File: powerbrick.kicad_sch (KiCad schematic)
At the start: 10 parts, among them J13 Conn_01x02_Socket, U4 LM2596S-3.3, U7 AMS1117-3.3

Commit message: .
.
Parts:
- added C18, C19, C20, C22, C23: 220nF/6,3V, Capacitor_SMD:C_0603_1608Metric, symbol Device:C
- added J17: Conn_01x02_Socket, Connector_JST:JST_XH_B2B-XH-A_1x02_P2.50mm_Vertical, symbol Connector:Conn_01x02_Socket
- added R13, R24, R25, R27: 10k, Resistor_SMD:R_0603_1608Metric, symbol Device:R
- added R26: 20k, Resistor_SMD:R_0603_1608Metric, symbol Device:R
- added TH1: Thermistor_NTC, Resistor_THT:R_Axial_DIN0204_L3.6mm_D1.6mm_P2.54mm_Vertical, symbol Device:Thermistor_NTC
- added U11, U13: AMS1117-3.3, Package_TO_SOT_SMD:SOT-223-3_TabPin2, symbol Regulator_Linear:AMS1117-3.3
- added U12: TP4056-42-ESOP8, Package_SO:SOIC-8-1EP_3.9x4.9mm_P1.27mm_EP2.41x3.3mm_ThermalVias, symbol Battery_Management:TP4056-42-ESOP8
- J13: footprint (none) -> Connector_Phoenix_MC:PhoenixContact_MC_1,5_2-GF-3.5_1x02_P3.50mm_Horizontal_ThreadedFlange_MountHole
- L1: value L -> 33uH; footprint (none) -> Inductor_SMD:L_7.3x7.3_H4.5
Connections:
- net +3.3V: now also C19.1, C23.1, U11.2 (VO), U13.2 (VO)
- net +5V: now also R24.1, R27.1, U12.4 (V_{CC}), U12.8 (CE)
- net GND: now also C18.2, C19.2, C20.2, C22.2, C23.2, J17.2 (Pin_2), R13.2, R25.2, R26.2, TH1.2, U11.1 (GND), U12.3 (GND), U12.9 (EPAD), U13.1 (GND)
- new net: R24.2, R25.1, TH1.1, U12.1 (TEMP)
- new net: R13.1, U12.2 (PROG)
- new net +BATT: C18.1, C20.1, C22.1, J17.1 (Pin_1), U11.3 (VI), U12.5 (BAT), U13.3 (VI)
- new net Vbat: R26.1, R27.2

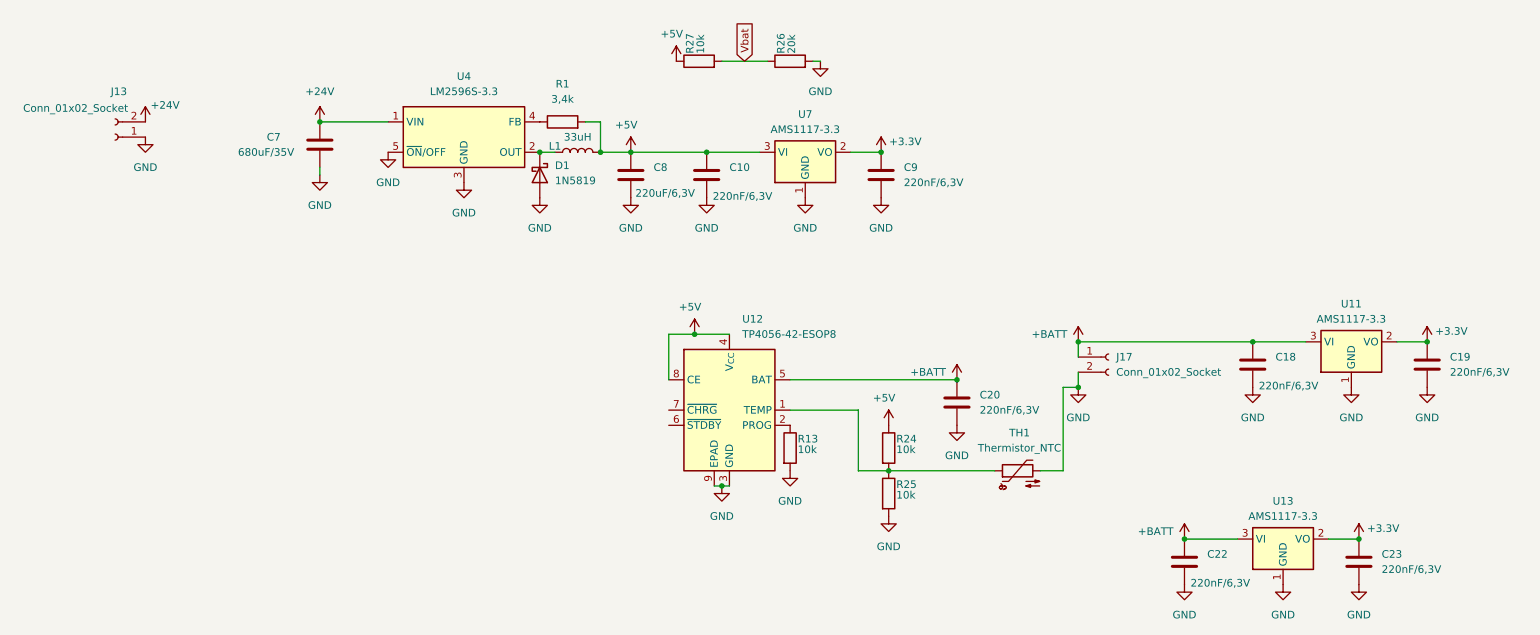
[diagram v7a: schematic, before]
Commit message: RIP
reason of death
too much of board for too little time...
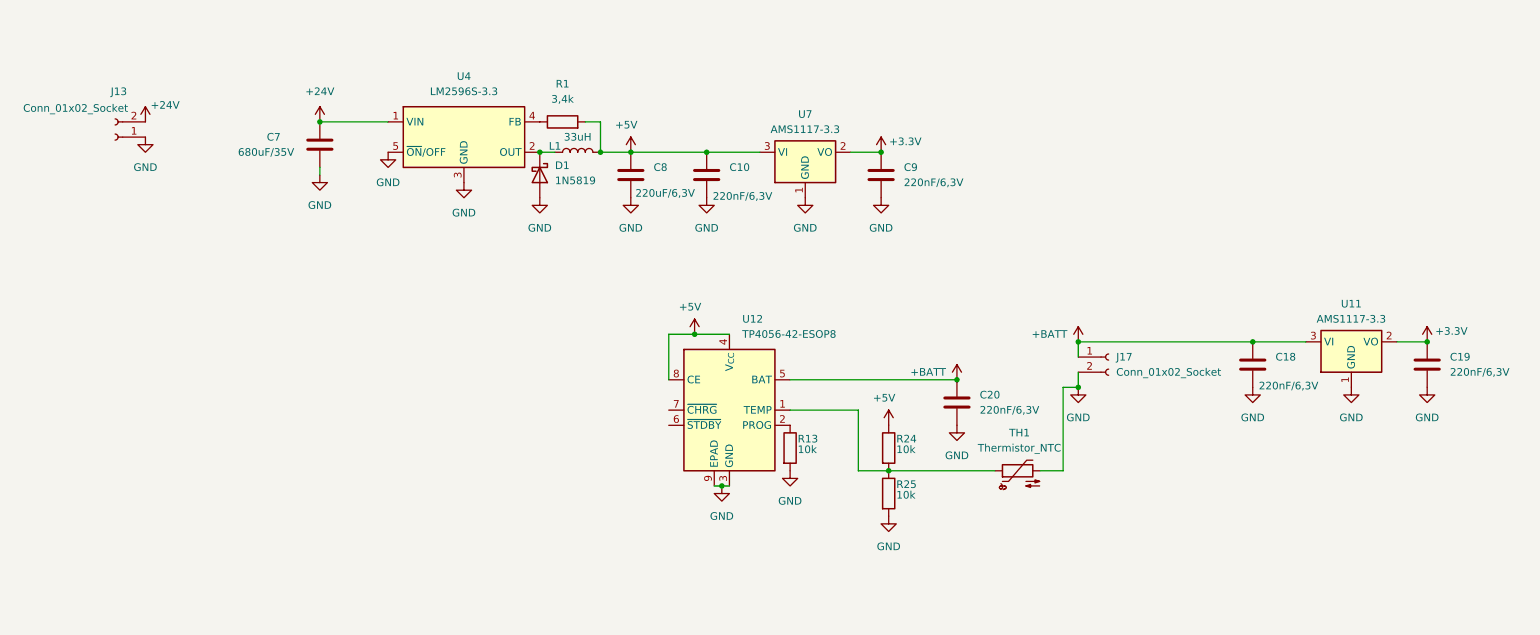
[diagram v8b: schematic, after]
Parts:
- removed C22, C23: 220nF/6,3V, Capacitor_SMD:C_0603_1608Metric, symbol Device:C
- removed R26: 20k, Resistor_SMD:R_0603_1608Metric, symbol Device:R
- removed R27: 10k, Resistor_SMD:R_0603_1608Metric, symbol Device:R
- removed U13: AMS1117-3.3, Package_TO_SOT_SMD:SOT-223-3_TabPin2, symbol Regulator_Linear:AMS1117-3.3
